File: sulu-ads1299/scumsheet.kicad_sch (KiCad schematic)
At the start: 25 parts, among them J10 through_hole, J11 through_hole, J12 through_hole, J13 through_hole, J14 through_hole, J15 through_hole, J16 through_hole, J17 through_hole, J18 through_hole, J19 through_hole, J20 through_hole, J21 through_hole, J22 through_hole, J23 through_hole, J24 through_hole, J25 through_hole, J9 through_hole, U5 scum3

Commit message: Sulu-ADS1299 started revision 2, added Molex libs, Banana for scale
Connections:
- net +VDDIO is gone; now on net +1.8V_REG: U5.36 (VDDIO)
- net BOOT_SOURCE_SEL is gone; now on net +1.1V_REG: U5.61 (BOOT_SOURCE_SELECT)
- net +VBAT renamed +1.8V_REG
- net +VDDD renamed +1.1V_REG
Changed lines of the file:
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@@
+    (stroke (width 0) (type default) (color 0 0 0 0))
+  )
+  (wire (pts (xy 130.81 15.24) (xy 132.08 15.24))
     (stroke (width 0) (type default) (color 0 0 0 0))
   )
@@
     (stroke (width 0) (type default) (color 0 0 0 0))
   )
+  (wire (pts (xy 209.55 102.87) (xy 214.63 102.87))
+    (stroke (width 0) (type default) (color 0 0 0 0))
+  )
   (wire (pts (xy 238.76 66.04) (xy 245.11 66.04))
     (stroke (width 0) (type default) (color 0 0 0 0))
   )
+  (wire (pts (xy 130.81 153.67) (xy 130.81 154.94))
+    (stroke (width 0) (type default) (color 0 0 0 0))
+  )
+  (wire (pts (xy 209.55 99.06) (xy 214.63 99.06))
+    (stroke (width 0) (type default) (color 0 0 0 0))
+  )
+  (wire (pts (xy 60.96 62.23) (xy 63.5 62.23))
+    (stroke (width 0) (type default) (color 0 0 0 0))
+  )
   (wire (pts (xy 129.54 29.21) (xy 129.54 17.78))
     (stroke (width 0) (type default) (color 0 0 0 0))
@@
     (stroke (width 0) (type default) (color 0 0 0 0))
   )
+  (wire (pts (xy 132.08 15.24) (xy 132.08 17.78))
+    (stroke (width 0) (type default) (color 0 0 0 0))
+  )
   (wire (pts (xy 132.08 17.78) (xy 129.54 17.78))
     (stroke (width 0) (type default) (color 0 0 0 0))
   )
-  (wire (pts (xy 245.11 60.96) (xy 250.19 60.96))
+  (wire (pts (xy 245.11 60.96) (xy 252.73 60.96))
     (stroke (width 0) (type default) (color 0 0 0 0))
   )
@@
     (effects (font (size 1.27 1.27)) (justify right))
   )
+  (hierarchical_label "+1.8V_REG" (shape input) (at 130.81 154.94 270)
+    (effects (font (size 1.27 1.27)) (justify right))
+  )
   (hierarchical_label "3WB_CLK" (shape bidirectional) (at 177.8 153.67 270)
+    (effects (font (size 1.27 1.27)) (justify right))
+  )
+  (hierarchical_label "+1.8V_REG" (shape input) (at 60.96 62.23 180)
     (effects (font (size 1.27 1.27)) (justify right))
   )
@@
     (effects (font (size 1.27 1.27)) (justify right))
   )
+  (hierarchical_label "+1.8V_REG" (shape input) (at 214.63 99.06 0)
+    (effects (font (size 1.27 1.27)) (justify left))
+  )
   (hierarchical_label "GPIO4" (shape bidirectional) (at 115.57 153.67 270)
     (effects (font (size 1.27 1.27)) (justify right))
@@
   (hierarchical_label "GPIO0" (shape bidirectional) (at 100.33 153.67 270)
     (effects (font (size 1.27 1.27)) (justify right))
-  )
-  (hierarchical_label "BOOT_SOURCE_SEL" (shape bidirectional) (at 209.55 102.87 0)
-    (effects (font (size 1.27 1.27)) (justify left))
   )
   (hierarchical_label "3WB_DATA" (shape bidirectional) (at 185.42 153.67 270)
@@
     (effects (font (size 1.27 1.27)) (justify left))
   )
+  (hierarchical_label "+1.1V_REG" (shape input) (at 130.81 15.24 180)
+    (effects (font (size 1.27 1.27)) (justify right))
+  )
   (hierarchical_label "GPIO11" (shape bidirectional) (at 146.05 153.67 270)
     (effects (font (size 1.27 1.27)) (justify right))
@@
     (effects (font (size 1.27 1.27)) (justify left))
   )
+  (hierarchical_label "+1.1V_REG" (shape input) (at 214.63 102.87 0)
+    (effects (font (size 1.27 1.27)) (justify left))
+  )
+  (hierarchical_label "+1.1V_REG" (shape input) (at 252.73 60.96 0)
+    (effects (font (size 1.27 1.27)) (justify left))
+  )
   (hierarchical_label "GPIO3" (shape bidirectional) (at 111.76 153.67 270)
     (effects (font (size 1.27 1.27)) (justify right))
@@
     )
     (property "Datasheet" "" (id 3) (at 232.41 73.66 0)
-      (effects (font (size 1.27 1.27)) hide)
-    )
-    (pin "1")
-  )
-  (symbol (lib_id "draft1library:+VDDIO") (at 130.81 153.67 180) (unit 1)
-    (in_bom yes) (on_board yes)
-    (property "Reference" "#PWR0107" (id 0) (at 130.81 149.86 0)
-      (effects (font (size 1.27 1.27)) hide)
-    )
-    (property "Value" "+VDDIO" (id 1) (at 130.81 160.02 90))
-    (property "Footprint" "" (id 2) (at 130.81 153.67 0)
-      (effects (font (size 1.27 1.27)) hide)
-    )
-    (property "Datasheet" "" (id 3) (at 130.81 153.67 0)
       (effects (font (size 1.27 1.27)) hide)
     )
@@
     (pin "2")
   )
-  (symbol (lib_id "draft1library:+VBAT") (at 209.55 99.06 270) (unit 1)
-    (in_bom yes) (on_board yes)
-    (property "Reference" "#PWR096" (id 0) (at 205.74 99.06 0)
-      (effects (font (size 1.27 1.27)) hide)
-    )
-    (property "Value" "+VBAT" (id 1) (at 212.8012 99.441 90)
-      (effects (font (size 1.27 1.27)) (justify left))
-    )
-    (property "Footprint" "" (id 2) (at 209.55 99.06 0)
-      (effects (font (size 1.27 1.27)) hide)
-    )
-    (property "Datasheet" "" (id 3) (at 209.55 99.06 0)
-      (effects (font (size 1.27 1.27)) hide)
-    )
-    (pin "1")
-  )
   (symbol (lib_id "draft1library:through_hole") (at 63.5 127 180) (unit 1)
     (in_bom yes) (on_board yes)
@@
     (pin "1")
   )
-  (symbol (lib_id "draft1library:+VDDD") (at 132.08 17.78 0) (unit 1)
-    (in_bom yes) (on_board yes)
-    (property "Reference" "#PWR084" (id 0) (at 132.08 21.59 0)
-      (effects (font (size 1.27 1.27)) hide)
-    )
-    (property "Value" "+VDDD" (id 1) (at 132.461 13.3858 0))
-    (property "Footprint" "" (id 2) (at 132.08 17.78 0)
-      (effects (font (size 1.27 1.27)) hide)
-    )
-    (property "Datasheet" "" (id 3) (at 132.08 17.78 0)
-      (effects (font (size 1.27 1.27)) hide)
-    )
-    (pin "1")
-  )
   (symbol (lib_id "draft1library:through_hole") (at 63.5 58.42 180) (unit 1)
     (in_bom yes) (on_board yes)
@@
     )
     (property "Datasheet" "" (id 3) (at 63.5 66.04 0)
-      (effects (font (size 1.27 1.27)) hide)
-    )
-    (pin "1")
-  )
-  (symbol (lib_id "draft1library:+VBAT") (at 63.5 62.23 90) (unit 1)
-    (in_bom yes) (on_board yes)
-    (property "Reference" "#PWR088" (id 0) (at 67.31 62.23 0)
-      (effects (font (size 1.27 1.27)) hide)
-    )
-    (property "Value" "+VBAT" (id 1) (at 60.2488 61.849 90)
-      (effects (font (size 1.27 1.27)) (justify left))
-    )
-    (property "Footprint" "" (id 2) (at 63.5 62.23 0)
-      (effects (font (size 1.27 1.27)) hide)
-    )
-    (property "Datasheet" "" (id 3) (at 63.5 62.23 0)
       (effects (font (size 1.27 1.27)) hide)
     )
@@
     (pin "2")
   )
-  (symbol (lib_id "draft1library:+VDDD") (at 250.19 60.96 270) (unit 1)
-    (in_bom yes) (on_board yes)
-    (property "Reference" "#PWR087" (id 0) (at 246.38 60.96 0)
-      (effects (font (size 1.27 1.27)) hide)
-    )
-    (property "Value" "+VDDD" (id 1) (at 255.905 60.325 90))
-    (property "Footprint" "" (id 2) (at 250.19 60.96 0)
-      (effects (font (size 1.27 1.27)) hide)
-    )
-    (property "Datasheet" "" (id 3) (at 250.19 60.96 0)
-      (effects (font (size 1.27 1.27)) hide)
-    )
-    (pin "1")
-  )
   (symbol (lib_id "draft1library:through_hole") (at 63.5 123.19 180) (unit 1)

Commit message: Updated sulu-ads1299 rev2 layout and schematic
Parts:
- renumbered C21 to C26, C22 to C27, C23 to C28, C24 to C29, C25 to C30, J13 to J10, J14 to J11, J15 to J12, J16 to J13, J17 to J14, J18 to J15, J19 to J16, J20 to J17, J21 to J18, J22 to J19, J23 to J20, J24 to J21, J25 to J22, J9 to J6, J10 to J7, J11 to J8, J12 to J9, R5 to R11, R6 to R12

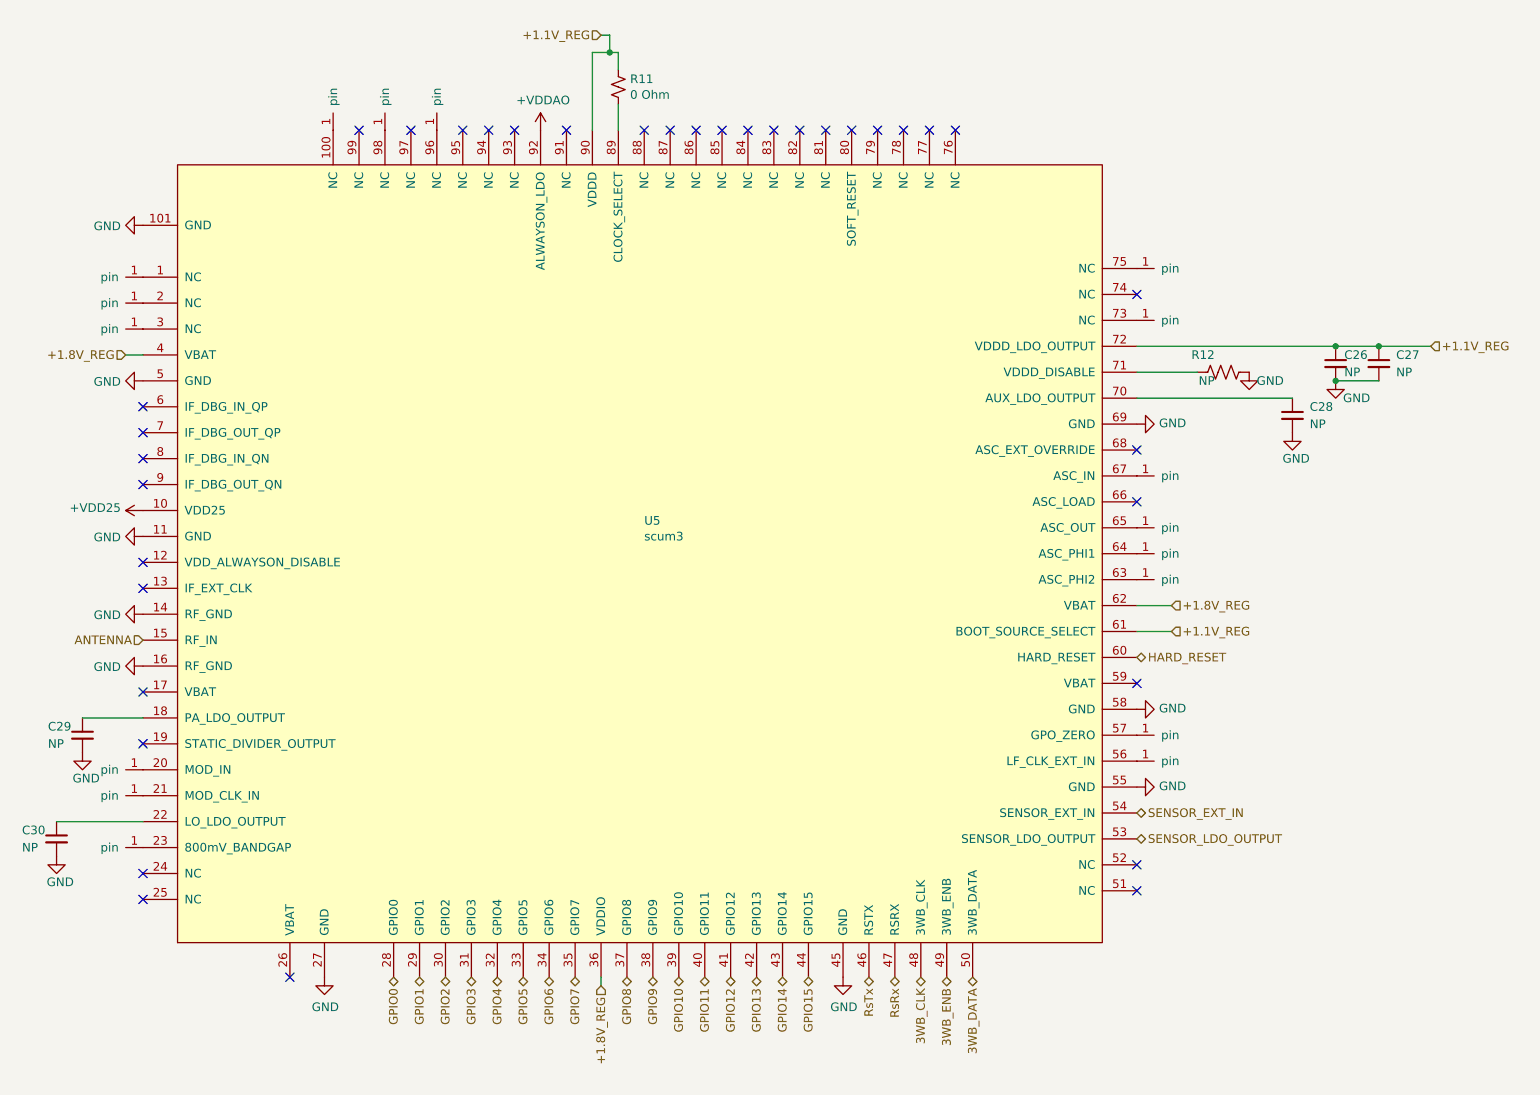
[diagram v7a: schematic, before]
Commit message: Sulu-ADS1299 components placed, new antenna, some routing
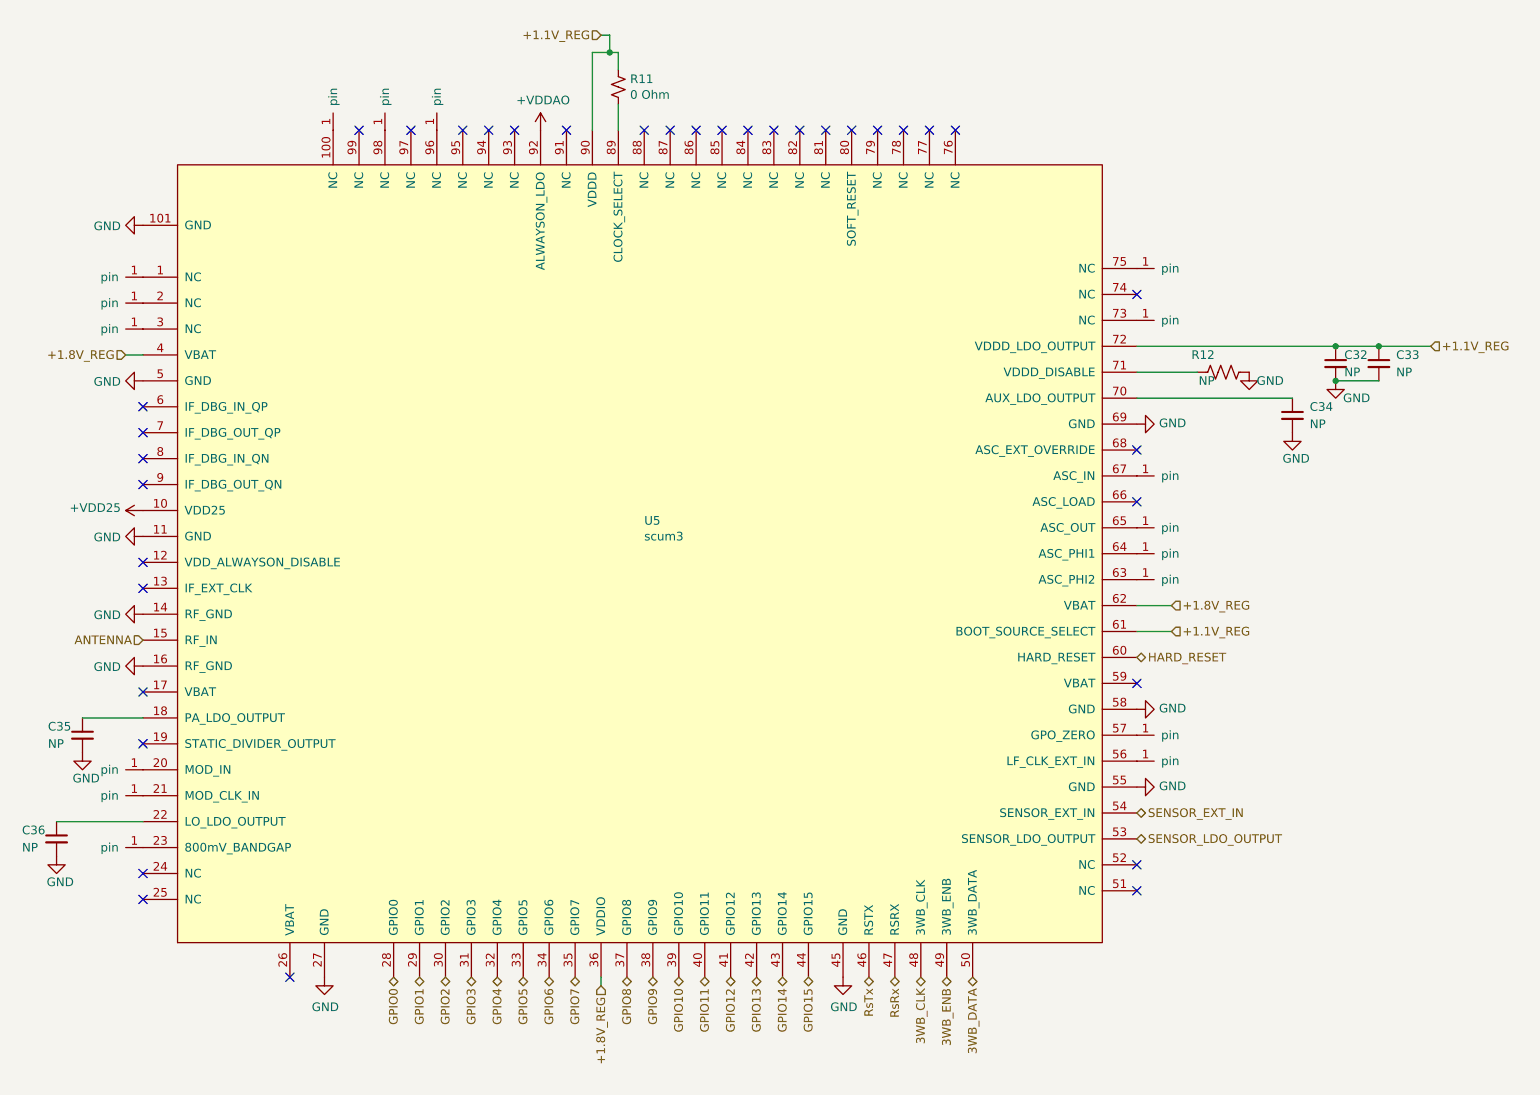
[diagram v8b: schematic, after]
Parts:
- renumbered C26 to C32, C27 to C33, C28 to C34, C29 to C35, C30 to C36
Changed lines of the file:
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@@
   (symbol (lib_id "power:GND") (at 232.41 73.66 0) (unit 1)
     (in_bom yes) (on_board yes)
-    (property "Reference" "#PWR069" (id 0) (at 232.41 80.01 0)
+    (property "Reference" "#PWR072" (id 0) (at 232.41 80.01 0)
       (effects (font (size 1.27 1.27)) hide)
     )
@@
   (symbol (lib_id "power:GND") (at 238.76 66.04 0) (unit 1)
     (in_bom yes) (on_board yes)
-    (property "Reference" "#PWR067" (id 0) (at 238.76 72.39 0)
+    (property "Reference" "#PWR070" (id 0) (at 238.76 72.39 0)
       (effects (font (size 1.27 1.27)) hide)
     )
@@
   (symbol (lib_id "power:GND") (at 209.55 125.73 90) (unit 1)
     (in_bom yes) (on_board yes)
-    (property "Reference" "#PWR076" (id 0) (at 215.9 125.73 0)
+    (property "Reference" "#PWR079" (id 0) (at 215.9 125.73 0)
       (effects (font (size 1.27 1.27)) hide)
     )
@@
   (symbol (lib_id "power:GND") (at 54.61 120.65 0) (unit 1)
     (in_bom yes) (on_board yes)
-    (property "Reference" "#PWR075" (id 0) (at 54.61 127 0)
+    (property "Reference" "#PWR078" (id 0) (at 54.61 127 0)
       (effects (font (size 1.27 1.27)) hide)
     )
@@
   (symbol (lib_id "power:GND") (at 63.5 100.33 270) (unit 1)
     (in_bom yes) (on_board yes)
-    (property "Reference" "#PWR072" (id 0) (at 57.15 100.33 0)
+    (property "Reference" "#PWR075" (id 0) (at 57.15 100.33 0)
       (effects (font (size 1.27 1.27)) hide)
     )
@@
   (symbol (lib_id "power:GND") (at 209.55 72.39 90) (unit 1)
     (in_bom yes) (on_board yes)
-    (property "Reference" "#PWR068" (id 0) (at 215.9 72.39 0)
+    (property "Reference" "#PWR071" (id 0) (at 215.9 72.39 0)
       (effects (font (size 1.27 1.27)) hide)
     )
@@
   (symbol (lib_id "power:GND") (at 209.55 114.3 90) (unit 1)
     (in_bom yes) (on_board yes)
-    (property "Reference" "#PWR074" (id 0) (at 215.9 114.3 0)
+    (property "Reference" "#PWR077" (id 0) (at 215.9 114.3 0)
       (effects (font (size 1.27 1.27)) hide)
     )
@@
   (symbol (lib_id "draft1library:+VDDAO") (at 121.92 29.21 0) (unit 1)
     (in_bom yes) (on_board yes)
-    (property "Reference" "#PWR063" (id 0) (at 121.92 33.02 0)
+    (property "Reference" "#PWR066" (id 0) (at 121.92 33.02 0)
       (effects (font (size 1.27 1.27)) hide)
     )
@@
   (symbol (lib_id "Device:C_Small") (at 245.11 63.5 0) (unit 1)
     (in_bom yes) (on_board yes) (fields_autoplaced)
-    (property "Reference" "C27" (id 0) (at 247.65 62.2362 0)
+    (property "Reference" "C33" (id 0) (at 247.65 62.2362 0)
       (effects (font (size 1.27 1.27)) (justify left))
     )
@@
   (symbol (lib_id "power:GND") (at 90.17 153.67 0) (unit 1)
     (in_bom yes) (on_board yes)
-    (property "Reference" "#PWR078" (id 0) (at 90.17 160.02 0)
+    (property "Reference" "#PWR081" (id 0) (at 90.17 160.02 0)
       (effects (font (size 1.27 1.27)) hide)
     )
@@
   (symbol (lib_id "power:GND") (at 63.5 66.04 270) (unit 1)
     (in_bom yes) (on_board yes)
-    (property "Reference" "#PWR066" (id 0) (at 57.15 66.04 0)
+    (property "Reference" "#PWR069" (id 0) (at 57.15 66.04 0)
       (effects (font (size 1.27 1.27)) hide)
     )
@@
   (symbol (lib_id "power:GND") (at 166.37 153.67 0) (unit 1)
     (in_bom yes) (on_board yes)
-    (property "Reference" "#PWR079" (id 0) (at 166.37 160.02 0)
+    (property "Reference" "#PWR082" (id 0) (at 166.37 160.02 0)
       (effects (font (size 1.27 1.27)) hide)
     )
@@
   (symbol (lib_id "Device:C_Small") (at 238.76 63.5 0) (unit 1)
     (in_bom yes) (on_board yes)
-    (property "Reference" "C26" (id 0) (at 240.03 62.23 0)
+    (property "Reference" "C32" (id 0) (at 240.03 62.23 0)
       (effects (font (size 1.27 1.27)) (justify left))
     )
@@
   (symbol (lib_id "Device:C_Small") (at 50.8 133.35 0) (unit 1)
     (in_bom yes) (on_board yes)
-    (property "Reference" "C30" (id 0) (at 45.72 132.08 0)
+    (property "Reference" "C36" (id 0) (at 45.72 132.08 0)
       (effects (font (size 1.27 1.27)) (justify left))
     )
@@
   (symbol (lib_id "power:GND") (at 63.5 43.18 270) (unit 1)
     (in_bom yes) (on_board yes)
-    (property "Reference" "#PWR064" (id 0) (at 57.15 43.18 0)
+    (property "Reference" "#PWR067" (id 0) (at 57.15 43.18 0)
       (effects (font (size 1.27 1.27)) hide)
     )
@@
   (symbol (lib_id "power:GND") (at 50.8 135.89 0) (unit 1)
     (in_bom yes) (on_board yes)
-    (property "Reference" "#PWR077" (id 0) (at 50.8 142.24 0)
+    (property "Reference" "#PWR080" (id 0) (at 50.8 142.24 0)
       (effects (font (size 1.27 1.27)) hide)
     )
@@
   (symbol (lib_id "draft1library:+VDD25") (at 63.5 85.09 90) (unit 1)
     (in_bom yes) (on_board yes)
-    (property "Reference" "#PWR070" (id 0) (at 67.31 85.09 0)
+    (property "Reference" "#PWR073" (id 0) (at 67.31 85.09 0)
       (effects (font (size 1.27 1.27)) hide)
     )
@@
   (symbol (lib_id "power:GND") (at 63.5 88.9 270) (unit 1)
     (in_bom yes) (on_board yes)
-    (property "Reference" "#PWR071" (id 0) (at 57.15 88.9 0)
+    (property "Reference" "#PWR074" (id 0) (at 57.15 88.9 0)
       (effects (font (size 1.27 1.27)) hide)
     )
@@
   (symbol (lib_id "Device:C_Small") (at 232.41 71.12 0) (unit 1)
     (in_bom yes) (on_board yes) (fields_autoplaced)
-    (property "Reference" "C28" (id 0) (at 234.95 69.8562 0)
+    (property "Reference" "C34" (id 0) (at 234.95 69.8562 0)
       (effects (font (size 1.27 1.27)) (justify left))
     )
@@
   (symbol (lib_id "power:GND") (at 63.5 107.95 270) (unit 1)
     (in_bom yes) (on_board yes)
-    (property "Reference" "#PWR073" (id 0) (at 57.15 107.95 0)
+    (property "Reference" "#PWR076" (id 0) (at 57.15 107.95 0)
       (effects (font (size 1.27 1.27)) hide)
     )
@@
   (symbol (lib_id "Device:C_Small") (at 54.61 118.11 0) (unit 1)
     (in_bom yes) (on_board yes)
-    (property "Reference" "C29" (id 0) (at 49.53 116.84 0)
+    (property "Reference" "C35" (id 0) (at 49.53 116.84 0)
       (effects (font (size 1.27 1.27)) (justify left))
     )
@@
   (symbol (lib_id "power:GND") (at 226.06 64.77 0) (unit 1)
     (in_bom yes) (on_board yes)
-    (property "Reference" "#PWR065" (id 0) (at 226.06 71.12 0)
-      (effects (font (size 1.27 1.27)) hide)
-    )
+    (property "Reference" "#PWR068" (id 0) (at 226.06 71.12 0)
+      (effects (font (size 1.27 1.27)) hide)
+    )
